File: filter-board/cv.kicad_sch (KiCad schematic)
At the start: 16 parts, among them U2 TL074

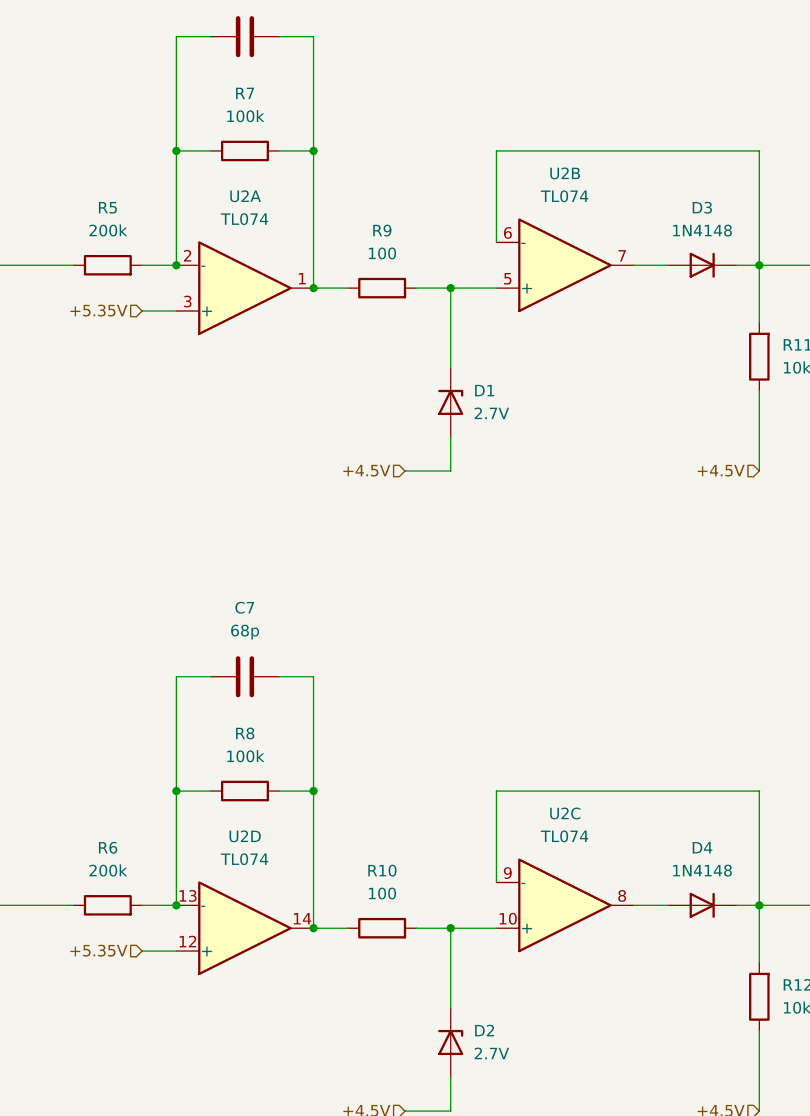
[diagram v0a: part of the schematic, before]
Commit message: Filter board layout
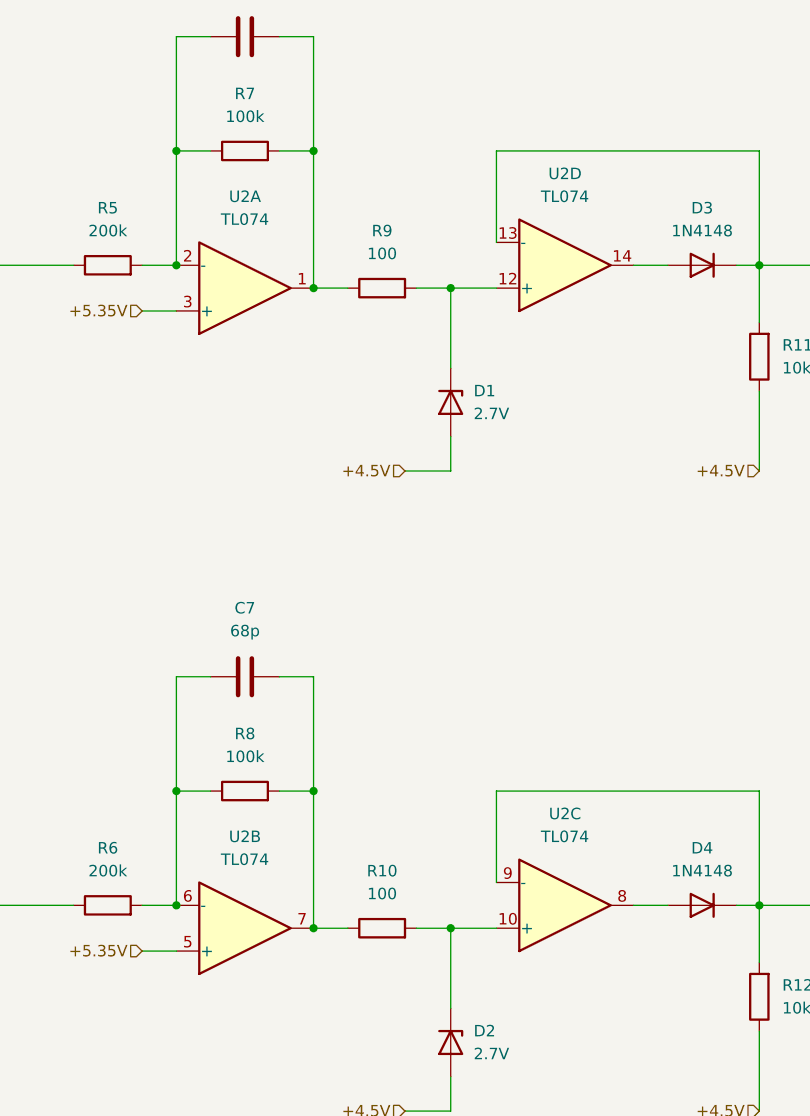
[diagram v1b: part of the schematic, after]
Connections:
- net +5.35V: now also U2.5 (+); no longer U2.12 (+)
- net Freq_CV_Biased: now also U2.13 (-); no longer U2.6 (-)
- net at C7.1, R6.2, R8.1: now also U2.6 (-); no longer U2.13 (-)
- net at C7.2, R10.1, R8.2: now also U2.7; no longer U2.14
- net at D3.2 (A): now also U2.14; no longer U2.7
- net at D1.1 (K), R9.2: now also U2.12 (+); no longer U2.5 (+)
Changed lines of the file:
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@@
     (pin "2")
   )
-  (symbol (lib_id "Amplifier_Operational:TL074") (at 119.38 50.8 0) (mirror x) (unit 2)
+  (symbol (lib_id "Amplifier_Operational:TL074") (at 119.38 50.8 0) (mirror x) (unit 4)
     (in_bom yes) (on_board yes) (fields_autoplaced)
     (property "Reference" "U2" (id 0) (at 119.38 40.64 0))
@@
     (pin "2")
   )
-  (symbol (lib_id "Amplifier_Operational:TL074") (at 83.82 124.46 0) (mirror x) (unit 4)
+  (symbol (lib_id "Amplifier_Operational:TL074") (at 83.82 124.46 0) (mirror x) (unit 2)
     (in_bom yes) (on_board yes) (fields_autoplaced)
     (property "Reference" "U2" (id 0) (at 83.82 114.3 0))

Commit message: wip
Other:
- note added: "Change R9 & R10 to 22k"
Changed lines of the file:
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@@
     (stroke (width 0) (type default) (color 0 0 0 0))
+  )
+  (text "Change R9 & R10 to 22k" (at 97.79 30.48 0)
+    (effects (font (size 1.27 1.27)) (justify left bottom))
   )
   (hierarchical_label "+4.5V" (shape input) (at 140.97 73.66 180)
